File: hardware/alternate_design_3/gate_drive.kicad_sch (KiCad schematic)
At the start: 34 parts, among them J1 Screw_Terminal_01x03, Q1 IRLZ44N, Q2 IRLZ44N, Q3 IRLZ44N, Q4 IRLZ44N, Q5 IRLZ44N, Q6 IRLZ44N, U5 ADUM3223ARZ, U6 ADUM3223ARZ, U7 ADUM3223ARZ

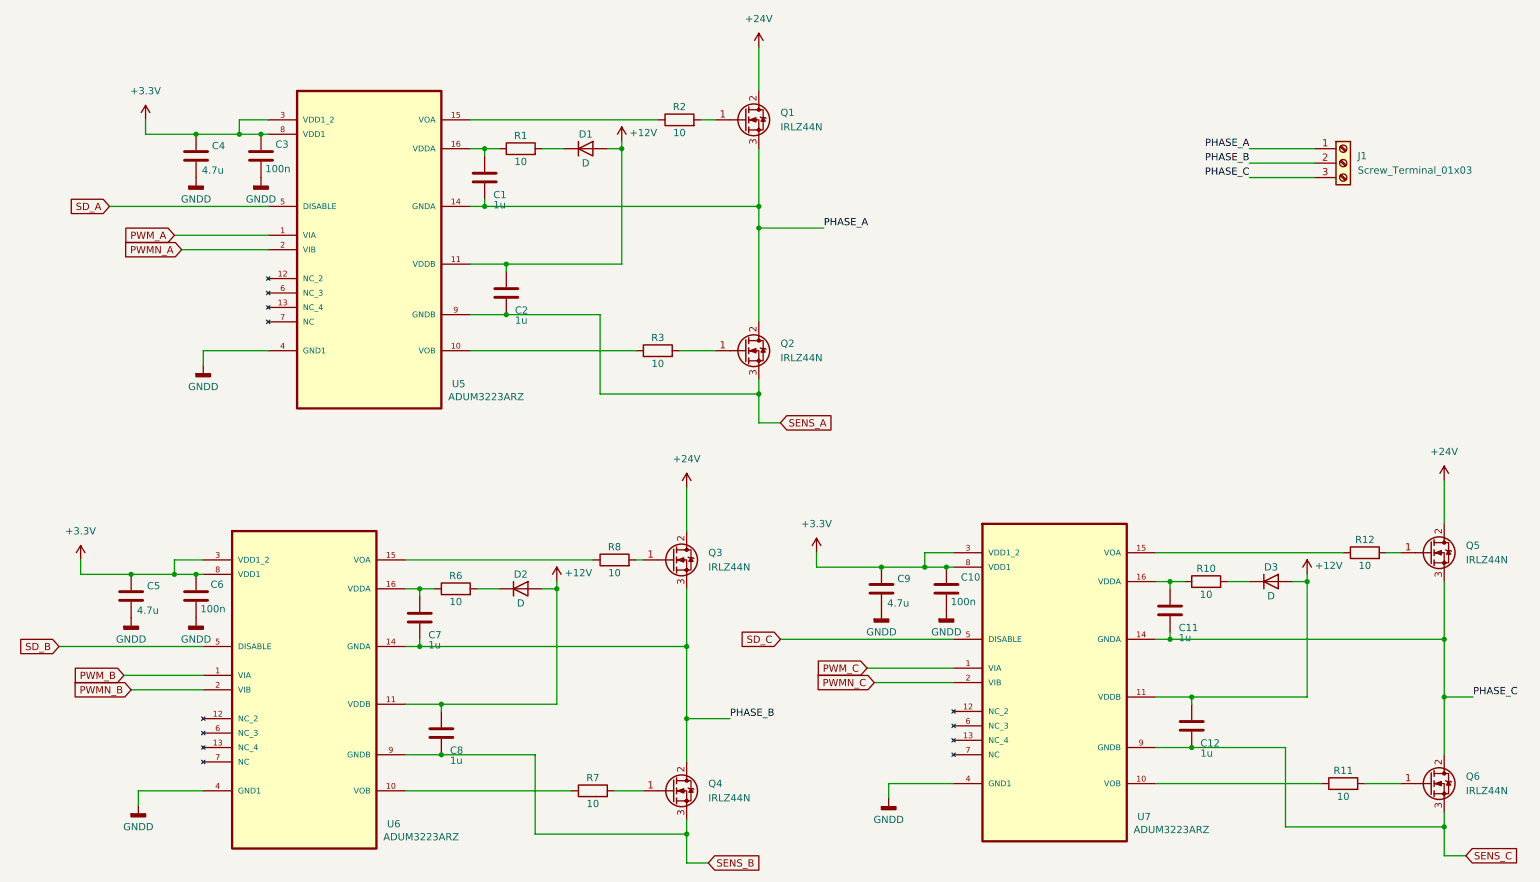
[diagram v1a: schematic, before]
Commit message: major additions to schematic of inverter
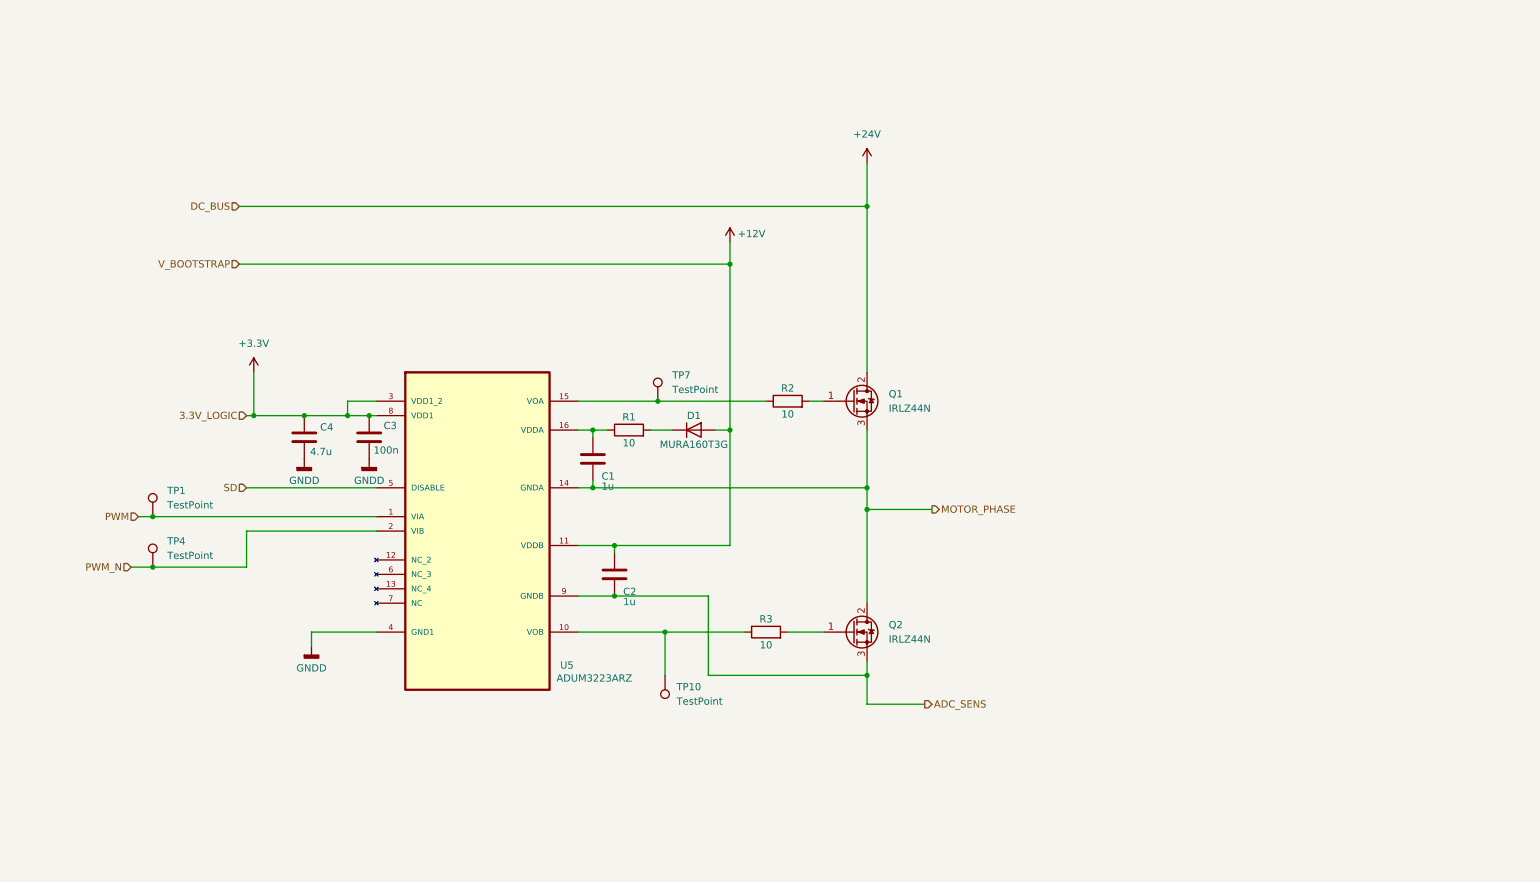
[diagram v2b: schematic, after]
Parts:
- removed C10, C6: 100n, symbol Device:C
- removed C11, C12, C7, C8: 1u, symbol Device:C
- removed C5, C9: 4.7u, symbol Device:C
- removed D2, D3: D, symbol Device:D
- removed J1: Screw_Terminal_01x03, symbol Connector:Screw_Terminal_01x03
- removed Q3, Q4, Q5, Q6: IRLZ44N, Package_TO_SOT_THT:TO-220-3_Vertical, symbol Transistor_FET:IRLZ44N
- removed R10, R11, R12, R6, R7, R8: 10, symbol Device:R
- removed U6, U7: ADUM3223ARZ, ADUM3223ARZ:SOIC127P600X175-16N, symbol ADUM3223ARZ:ADUM3223ARZ
- added TP1, TP10, TP4, TP7: TestPoint, symbol Connector:TestPoint
- D1: value D -> MURA160T3G
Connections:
- net at R3.1, U5.10 (VOB): now also TP10.1
- net at R2.1, U5.15 (VOA): now also TP7.1
- net PHASE_A renamed MOTOR_PHASE
- net PWMN_A renamed PWM_N
- net PWM_N: now also TP4.1
- net PWM_A renamed PWM
- net PWM: now also TP1.1
- net SD_A renamed SD
- net SENS_A renamed ADC_SENS
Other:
- moved on the sheet: C1, C2, C3, C4, D1, Q1, Q2, R1, R2, R3, U5
